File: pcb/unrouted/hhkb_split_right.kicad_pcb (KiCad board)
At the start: 2 copper layers, 173.7 x 97.4 mm, 83 parts, among them SW1 6, SW10 Y, SW11 U, SW12 I, SW13 O, SW14 P, SW15 [, SW16 ], SW17 Del, SW18 H, SW19 J, SW2 7, SW20 K, SW21 L, SW22 ;, SW23 ', SW24 Enter, SW25 N, SW26 M, SW27 ,, SW28 ., SW29 /, SW3 8, SW30 Shift, SW31 Fn, SW32 R-Space, SW33 Meta, SW34 Alt, SW4 9, SW5 0, SW6 -, SW7 =, SW8 \, SW9 `, U1 74LVC595, U2 74LVC595

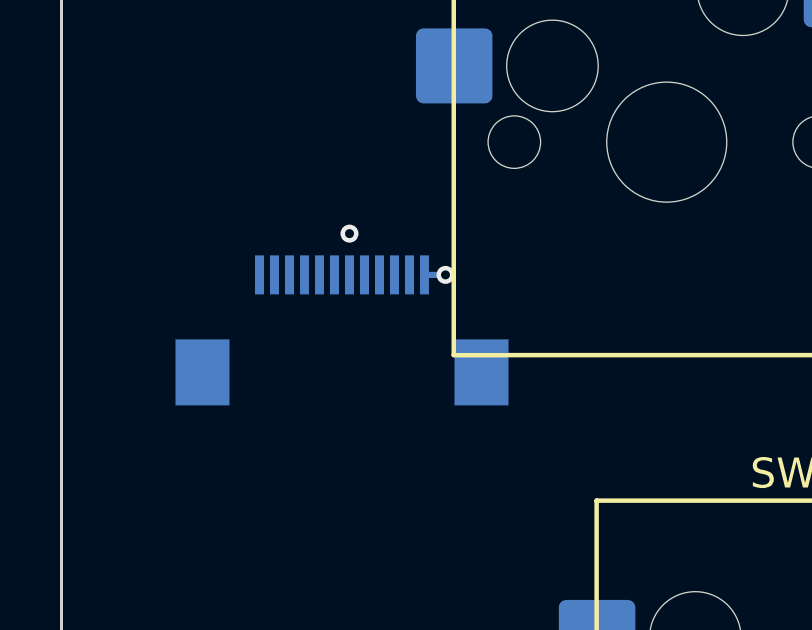
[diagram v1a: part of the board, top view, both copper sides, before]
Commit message: FFC コネクタの X を子基板と揃えた（左 3.52 → 0.40mm・右 1.35 → 0.00mm）
本体基板の J_DB と子基板の J_MAIN は**どちらも口が手前を向いている**のに
X がずれていて、ずれたぶん FFC が横へ折れていた（利用者の指摘）。

**座標を手で書かず、子基板の中心から取る。**直書きだとキー配列や
ケースの幅が動いた日に黙ってずれる。そのため
inner_sign / battery_x_center / daughterboard_x_center を gen_case.py
（build123d 依存で KiCad の Python から読めない）から interface.py へ移し、
gen_case は再輸出だけにした。二重に持っていた DB_W も出所を 1 つにし、
WALL / BATT_X は突き合わせの assert を置いた。

揃えた先に部品が居ることがあるので、_snap_clear_of_courtyards が
当たらない最寄りへ逃がし、ずれ量を印字する（左は D12 が 0.36mm 掛かるので
+0.40mm、右は 0.00mm で完全一致）。**スイッチは障害物に数えない**——
実装面が違う（スイッチは表・コネクタは裏の SMD）ので重なってよく、
数えると右が 3.95mm 逃げて揃える前より悪くなる。

## 一緒に見つかった別のバグ

GUIDE_VIAS の V3V3 中継ビアが (72.75, 84.0) と直書きされていた。
J_DB が動いた瞬間、**V3V3 のパッド(76.10)から外れて ROW_B のパッド(72.60)
の上に乗り**、ROW_B が未配線になる。パッドから座標を取るようにした。
これは移設前から潜在していたもので、実際にベースラインの右基板は
未配線 2 件（ROW_B と GND 離島）だった。

## 検証

- 再生成 → 自動配線 → DRC: 左 0/0・右 違反 0/未配線 1・子基板 0/0
  右の 1 件は U1 の GND 離島で、**ベースラインにもあった**（2 → 1 に減った）。
  コネクタ位置と無関係な既存の不具合なので範囲を広げず残す
- ずれ量は pcb_parts.json を取り直したうえで**実 STEP 形状から実測**
- gen_assembly の実形状の干渉 0 / refresh_view.sh で .blend も出し直し
- pytest tools: 437 passed / 3 failed。**3 件とも着手前から赤**
  （SPARE ネット 2 件は stash して確認済み、右の未配線 1 件は上記）

Co-Authored-By: Claude Opus 5 (1M context) <noreply@anthropic.com>
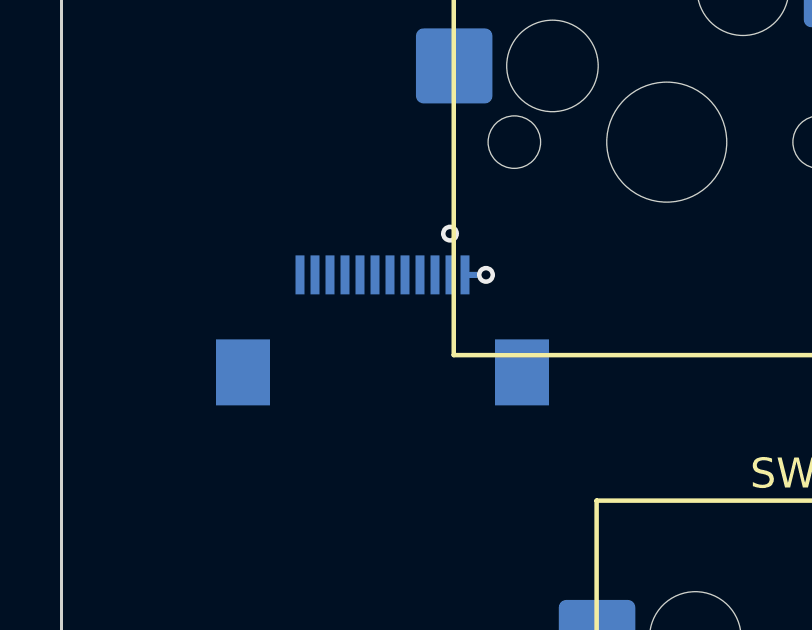
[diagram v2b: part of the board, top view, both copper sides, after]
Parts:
- moved J_DB 1.35 mm to (73.8, 87.2)

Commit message: 右の行とレーンの対応を左の鏡像に直した（ROW_A が最遠の行まで降りていた）
J_DB のパッド列は扇の根元で、外側(#12)を通る芯線が遠い行へ、内側(#8)が
近い行へ行くと交差しない。右はこの向きが左と同じままで、ROW_A(#8・最も
内側)が最遠の行(y=138.45)まで斜めに降り、ROW_E(#12)が束の真ん中に来て
いた。右の row-gpios を組み替えて、パッドの外側ほど遠い行になるようにした。

  #8 ROW_A → 行y 81.30 (コネクタから 4.08)
  #9 ROW_B → 100.35 (14.97)
  #10 ROW_C → 62.25 (23.12)
  #11 ROW_D → 119.40 (34.03)
  #12 ROW_E → 138.45 (53.07)

左は逆向きの単調で無変更。ネット名(#8=ROW_A…#12=ROW_E)は左右で同じで、
動かしたのは「どのレーンがどの行に載るか」だけ。circuit.py の J_DB は共通。

**未配線が 0 → 2 になったが、数字が悪いほうが正しい。**前の並びは未配線 0
だったが、扇が交差したまま通っていただけ。未配線 0 を根拠に戻さないこと。
残りは ROW_D(#11 → 行3) と GND(C_U2 のパッド 2 → ベタ・ROW とは別件)。

右の overlay には 2026-08-15 から「左とは意味が逆なので並びも逆になる」と
書いてあったが、実装が追随しておらず左と同一だった。文書だけが正しかった。

Co-Authored-By: Claude Opus 5 (1M context) <noreply@anthropic.com>
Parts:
- C_U1, C_U2: value cap_100n -> 100nF
- J_DB: value ffc_12p -> FH12-12S-0.5SH(55)
- SW1: value 6 -> CPG151101S11-2
- SW10: value Y -> CPG151101S11-2
- SW11: value U -> CPG151101S11-2
- SW12: value I -> CPG151101S11-2
- SW13: value O -> CPG151101S11-2
- SW14: value P -> CPG151101S11-2
- SW15: value [ -> CPG151101S11-2
- SW16: value ] -> CPG151101S11-2
- SW17: value Del -> CPG151101S11-2
- SW18: value H -> CPG151101S11-2
- SW19: value J -> CPG151101S11-2
- SW2: value 7 -> CPG151101S11-2
- SW20: value K -> CPG151101S11-2
- SW21: value L -> CPG151101S11-2
- SW22: value ; -> CPG151101S11-2
- SW23: value ' -> CPG151101S11-2
- SW24: value Enter -> CPG151101S11-2
- SW25: value N -> CPG151101S11-2
- SW26: value M -> CPG151101S11-2
- SW27: value , -> CPG151101S11-2
- SW28: value . -> CPG151101S11-2
- SW29: value / -> CPG151101S11-2
- SW3: value 8 -> CPG151101S11-2
- SW30: value Shift -> CPG151101S11-2
- SW31: value Fn -> CPG151101S11-2
- SW32: value R-Space -> CPG151101S11-2
- SW33: value Meta -> CPG151101S11-2
- SW34: value Alt -> CPG151101S11-2
- SW4: value 9 -> CPG151101S11-2
- SW5: value 0 -> CPG151101S11-2
- SW6: value - -> CPG151101S11-2
- SW7: value = -> CPG151101S11-2
- SW8: value \ -> CPG151101S11-2
- SW9: value ` -> CPG151101S11-2
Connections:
- D10 pad 1: ROW_E -> ROW_A
- D11 pad 1: ROW_E -> ROW_A
- D12 pad 1: ROW_E -> ROW_A
- D13 pad 1: ROW_E -> ROW_A
- D14 pad 1: ROW_E -> ROW_A
- D15 pad 1: ROW_E -> ROW_A
- D16 pad 1: ROW_E -> ROW_A
- D17 pad 1: ROW_E -> ROW_A
- D18 pad 1: ROW_D -> ROW_B
- D19 pad 1: ROW_D -> ROW_B
- D20 pad 1: ROW_D -> ROW_B
- D21 pad 1: ROW_D -> ROW_B
- D22 pad 1: ROW_D -> ROW_B
- D23 pad 1: ROW_D -> ROW_B
- D24 pad 1: ROW_D -> ROW_B
- D25 pad 1: ROW_B -> ROW_D
- D26 pad 1: ROW_B -> ROW_D
- D27 pad 1: ROW_B -> ROW_D
- D28 pad 1: ROW_B -> ROW_D
- D29 pad 1: ROW_B -> ROW_D
- D30 pad 1: ROW_B -> ROW_D
- D31 pad 1: ROW_B -> ROW_D
- D32 pad 1: ROW_A -> ROW_E
- D33 pad 1: ROW_A -> ROW_E
- D34 pad 1: ROW_A -> ROW_E
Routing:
- net ROW_E: track 138.1 -> 66.7 mm
- net ROW_A: track 66.7 -> 138.1 mm
- net ROW_D: track 126.2 -> 128.6 mm
- net ROW_B: track 128.6 -> 126.2 mm

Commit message: 右の段 1 の列割り当てを規則的に直した（配線ルールは触らない）
利用者「右は、まず配線ルールは基本いじらずに、まずは列割り当てを
直しましょう。明らかに規則的じゃない」。

**測ったら、4 段のうち段 1 だけが不規則だった。**

段 1（Y U I O P [ ] Del）は列 8 を飛ばして 6,7,9,10,11,12,13,14 に
していた。**8 キーとも 1u で等間隔なのに途中で 1 つ飛ばすと、I 以降が
全部 1 列ぶん右にずれる**。実測で 2 キーが「キーの真上を通らない列」に
繋がっていた:

    P  範囲 257.2〜276.2  真上は COL10 だけ  なのに COL11(276.2)
    [  範囲 276.2〜295.3  真上は COL11 だけ  なのに COL12(295.3)

**6〜12 を連続で使い、空けるのは 13** に変更。これで 8 キーとも真上の
列に乗る（6/8 → 8/8）。Del だけ 1.5u で右端に寄るので COL14。

**他の段（2/3/4）は総当りで測った結果すでに最良**で、飛ばしている列は
幅広キー（Enter 2.25u / Shift 1.75u / R-Space 3u）による本物の欠番
だった。**触らない。**

配線ルールは 1 文字も変えていない。それでも割り当てを直しただけで
**引けなかったホップが 4 → 3 に減った**（右: 列 83 → 92 区間）。
配線由来の DRC 違反 0。残る未接続はマトリクス内 2 件（COL7/COL8）と
GND の島 1 件。

左は変化なし（段 1 は右だけの行。指紋で確認して戻した）。

Co-Authored-By: Claude Opus 5 (1M context) <noreply@anthropic.com>
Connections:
- SW12 pad 1: COL3 -> COL2
- SW13 pad 1: COL4 -> COL3
- SW14 pad 1: COL5 -> COL4
- SW15 pad 1: COL6 -> COL5
- SW16 pad 1: COL7 -> COL6

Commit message: 右の列を「行内の順番＝列番号」にした（利用者の指定）
利用者「SW1, 10, 18, 25, 32 を Col 0 として。以降、その行を一つ右に
いくごとに列を増やして」「ただし SW33, 34 は例外」。

各行の左端が COL0、以降 +1。**飛ばさない。**以前は段ごとに開始列も
欠番もばらばらで（段2 は列 7 から、段4 は列 8 から、SW17 が COL8、
SW30 が COL7）、「行内の位置」と「列番号」が対応していなかった。

例外の SW33/SW34 は、実測でキーの真上を通る列に合わせた（確認済み）:
    SW33 Meta  範囲 247.65〜276.23 → COL3（x=261.94 と完全一致）
    SW34 Alt   範囲 276.23〜295.27 → COL4（ずれ 4.76mm）

**配線ルールは 1 文字も変えていない。**割り当てだけで、引けなかった
ホップが **4 → 2**、マトリクス内の未接続が **3 → 1** に減った
（右: 列 88 区間・橋のビア 38 個・配線由来の DRC 違反 0）。

## 検査を 1 つ作り直した

`test_matrix_columns_follow_physical_position`（同じ列のキーが x 方向に
1.5 キー幅以内）は、**この方針では必ず落ちる**——各行の左端が COL0 に
なるので同じ列が 38mm 散らばる。

**落ちるから外す、はしない。**守りたかったのは x の散らばりではなく
「長い横断が生まれないこと」（38mm の横断で DRC が交差を出した事故から
書かれた検査）なので、**そちらを直接測る**ように書き換えた
（`test_matrix_columns_do_not_need_long_crossings`）。実測の最長は
左 16.7mm / 右 20.2mm で、1 段ぶんの斜め（26.9mm）以内。

⚠️ **途中、正規表現が `(net <番号>)` を探していて 1 本も拾えず、
閾値を 15mm に下げても通っていた。**`(segment ...)` はネットを名前で
持つ。書式を実物で確かめて直し、**閾値を下げると落ちること**を
確認した（16.7 / 20.2mm が正しく出る）。読めなかったら落ちる
assert も足した。

本番の `pcb/` は古い割り当てのままなので
`test_matrix_wiring_matches_the_firmware` が赤。**意図した状態**として
open-gaps #47 に記録した（残り 6 件の赤は私の変更前から）。

Co-Authored-By: Claude Opus 5 (1M context) <noreply@anthropic.com>
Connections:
- SW17 pad 1: COL8 -> COL7
- SW18 pad 1: COL1 -> COL0
- SW19 pad 1: COL2 -> COL1
- SW20 pad 1: COL3 -> COL2
- SW21 pad 1: COL4 -> COL3
- SW22 pad 1: COL5 -> COL4
- SW23 pad 1: COL6 -> COL5
- SW24 pad 1: COL7 -> COL6
- SW25 pad 1: COL1 -> COL0
- SW26 pad 1: COL2 -> COL1
- SW27 pad 1: COL3 -> COL2
- SW28 pad 1: COL4 -> COL3
- SW29 pad 1: COL5 -> COL4
- SW30 pad 1: COL7 -> COL5
- SW31 pad 1: COL8 -> COL6
- SW32 pad 1: COL2 -> COL0
- SW33 pad 1: COL4 -> COL3
- SW34 pad 1: COL5 -> COL4

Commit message: 右のマトリクスを完成させた（U1/U2 の移動を取り込み・引き残し 0）
利用者が基板上で U2 と U1 を動かした:
  「SW6 から SW15 は U2 をずらしたので、それで試してください」
  「SW16-24 は工夫して」
  「SW5, 6 だけど、他の同じ行の配線パターンを踏襲して」
  「コンデンサとか避けておいたので」

**U1/U2 の移動を生成器へ取り込んだ**（座標が完全一致することを確認）:
  U2  帯0 x=+15.0    → 帯1 x=-40.662 dy=+0.725  (109.338, 88.900)
  U1  帯0 x=+2.0     → 帯3 x=-75.938 dy=-0.025  ( 74.062,126.250)

どちらも**列の通り道を塞いでいた**。U2 は COL5（SW6→SW15）を、
U1 と C_U1 は COL4（x≈146〜152）を。移動で両方とも素直に降りられる。

**SW5 が同じ段の他と揃った**（利用者の指摘）。SW4/SW5/SW6 が
「0.200mm 降りて曲がり、75.650 で 45° を終える」と完全に同じ形。
前は SW5 だけ 3.700mm 降りていた（U1/C_U1 を避けるため）。

**SW16→SW24（ST24 のスタビ穴）は形 F で解いた。**C も D も曲がる y が
1 点に決まっており、そこが穴の真横だと 0.289mm しか空かない。
**曲がる高さを振れる形**を足すと、45° を保ったまま穴の左を抜けて
1.030mm 取れる（他の列と同じ値）。

2 つ直した:
  - 橋を架ける枝でも**余裕が最大の候補を採る**（他の枝は済んでいた）
  - `gen_matrix` が **GND の離島を繋いでいなかった**。配線が密になって
    ベタが割れ、DRC が「ゾーンが繋がっていない」を 2 件出した。
    本番と同じ `gnd_fanout.stitch_islands` を呼ぶ（左 10 個・右 12 個）。
    浮いた銅は 2.4GHz でアンテナになる

左右とも: **引かなかったホップ 0 / 配線由来の DRC 違反 0 /
マトリクス内の未接続 0 / 最小の隙間 1.030mm**。

⚠️ **C_U1 は取り込んでいない。**利用者の板では U1 から 136mm 離れており、
パスコンとして効かない位置（効くのは往復ループのインダクタンス）。
`DECOUPLE_BESIDE` が U1 から算出する仕組みのまま残した。

pytest の赤 8 件は**私の変更の前後で同じ**（本番 pcb/ が未再生成＝
open-gaps #47、SPARE 系は以前から）。

Co-Authored-By: Claude Opus 5 (1M context) <noreply@anthropic.com>
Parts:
- moved C_U1 96.6 mm to (68.2, 126.2)
- moved U1 96.6 mm to (74.1, 126.2)
- moved C_U2 59.1 mm to (103.4, 88.9)
- moved U2 59.1 mm to (109.3, 88.9)

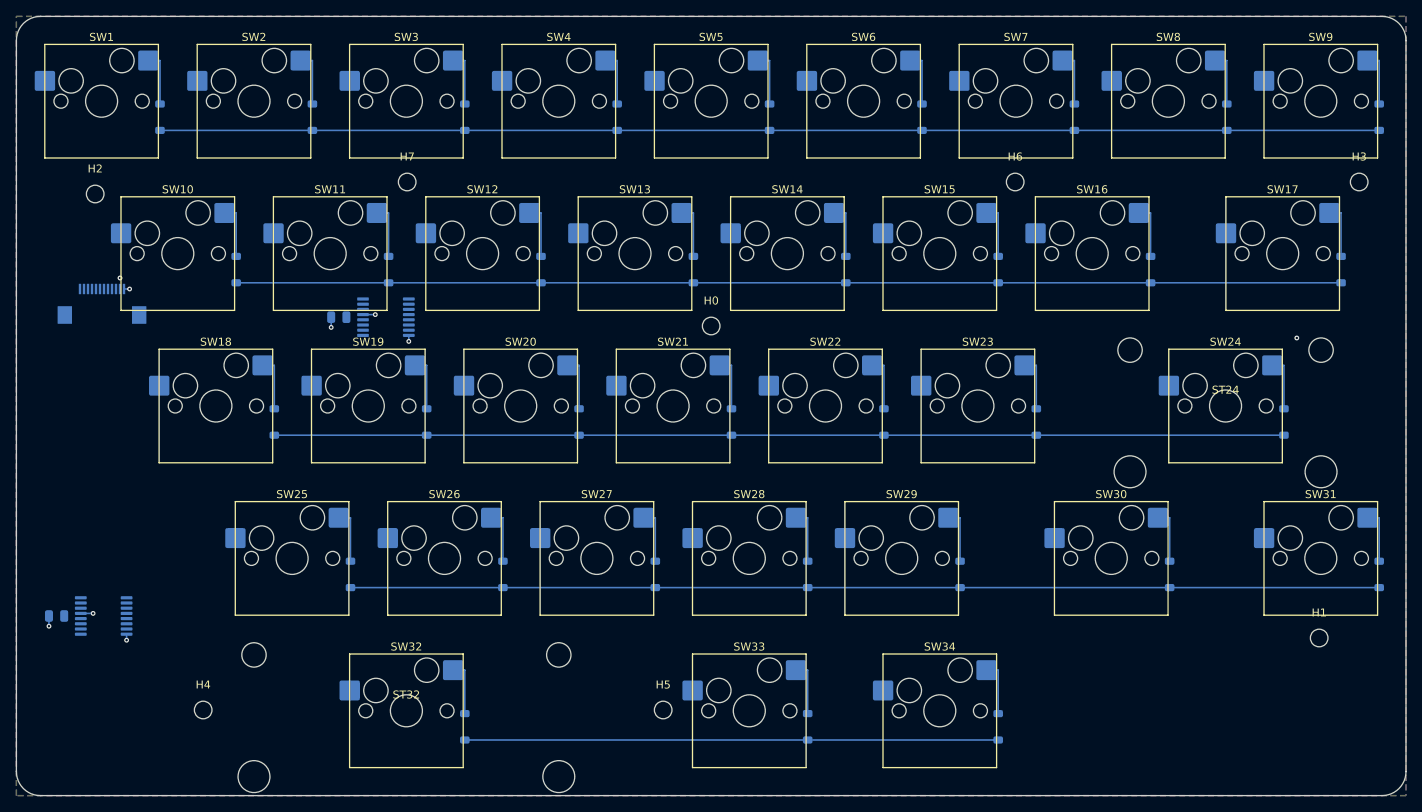
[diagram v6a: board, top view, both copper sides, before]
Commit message: キーマトリクスの配線を凍結した（自動配線の前に機械で引く）
利用者「このキーマトリクスの配線を凍結させてください。基本的にはこの
配線は変更せず、自動配線の前に機械的に配線しておく形にしておいて」。

  gen_pcb   … 列のバスも引く（行・SW→D に続いて 3 つ目）。
              左 99 区間 / 右 119 区間・**全ホップ**
  autoroute … SES 取り込みのあと `replay_matrix` で
              **未配線の板からそのまま写す**

## 「引き直す」ではなく「写す」にした理由

最初は取り込み後に `prewire_col_bus` を呼び直す形にした。**13 ホップが
「障害物」で落ちた。**経路は板の上にある物から決まるが、取り込み後は
ビアが 38 → 1217 個に増えている（gnd_fanout）。**同じ手順を回しても
同じ答えにならない。**

**凍結とは同じ手順を回すことではなく、同じ結果を置き直すこと。**
未配線の板が唯一の出どころで、そこに gen_pcb が引いた線が残っている。
実測で **209 個中 209 個が完全一致**（差分は両方向ともゼロ）。

## 注記と実物が食い違っていたのを直した

`_strip_prewired` の説明は「ROW は `(type protect)` で渡してある」と
書いていたが、**実際は `type route` のままだった**（COL も同じ）。
上の置換は「消したネット」にしか掛からず、消さない ROW/COL には
効いていなかった。`FROZEN` を足して明示的に protect にする。
ROW/COL をネットごと消せないのは、最後の 1 本（ROW は J_DB、
COL は U1）だけは Freerouting に引かせるため。

## 置き換えたものを消した

`tools/gen_matrix.py` と `pcb/matrix/` を削除（役目を gen_pcb が継いだ）。
長い横断の検査は `pcb/unrouted/` を見るように変更——**形が決まるのは
そこ**で、本番はその写し。消した名前で grep して残骸 0 を確認。
故意に閾値を下げて、検査が効いていることも確認（16.7 / 20.2mm）。

⚠️ **本番の pcb/ はまだ作り直していない**（利用者「本番配線はまだ。
U1, U2 の場所や配線が決まってから」）。open-gaps #47 を現状に合わせて
書き直した。pytest の赤 8 件は私の変更前と同じ顔ぶれ。

Co-Authored-By: Claude Opus 5 (1M context) <noreply@anthropic.com>
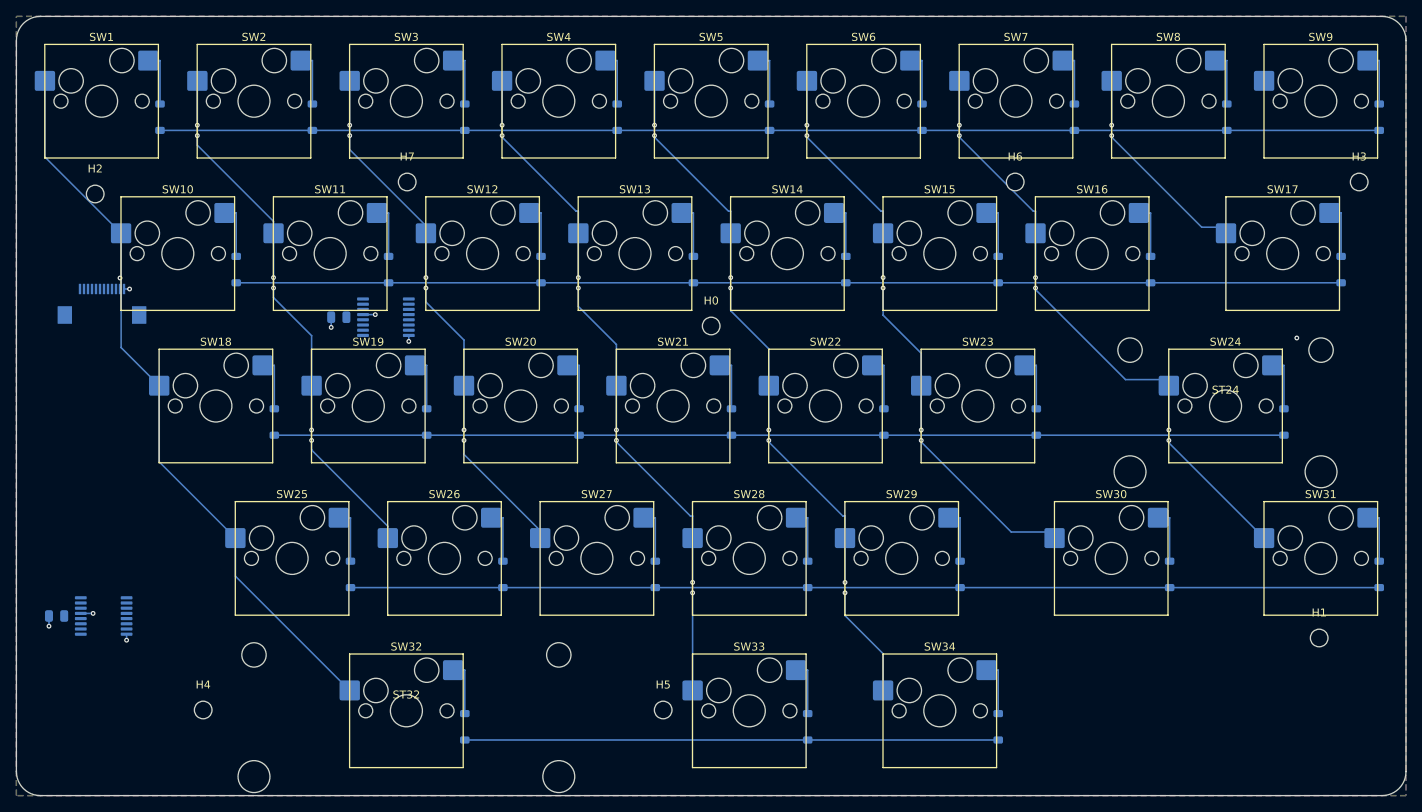
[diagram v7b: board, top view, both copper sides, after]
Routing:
- net COL0: track 0.00 -> 92.0 mm
- net COL4: track 0.00 -> 88.4 mm, vias 0 -> 8
- net COL3: track 0.00 -> 86.4 mm, vias 0 -> 8
- net COL6: track 0.00 -> 76.3 mm, vias 0 -> 6
- net COL5: track 0.00 -> 73.3 mm, vias 0 -> 6
- net COL2: track 0.00 -> 67.0 mm, vias 0 -> 6
- net COL1: track 0.00 -> 67.0 mm, vias 0 -> 6
- net COL7: track 0.00 -> 26.7 mm, vias 0 -> 2

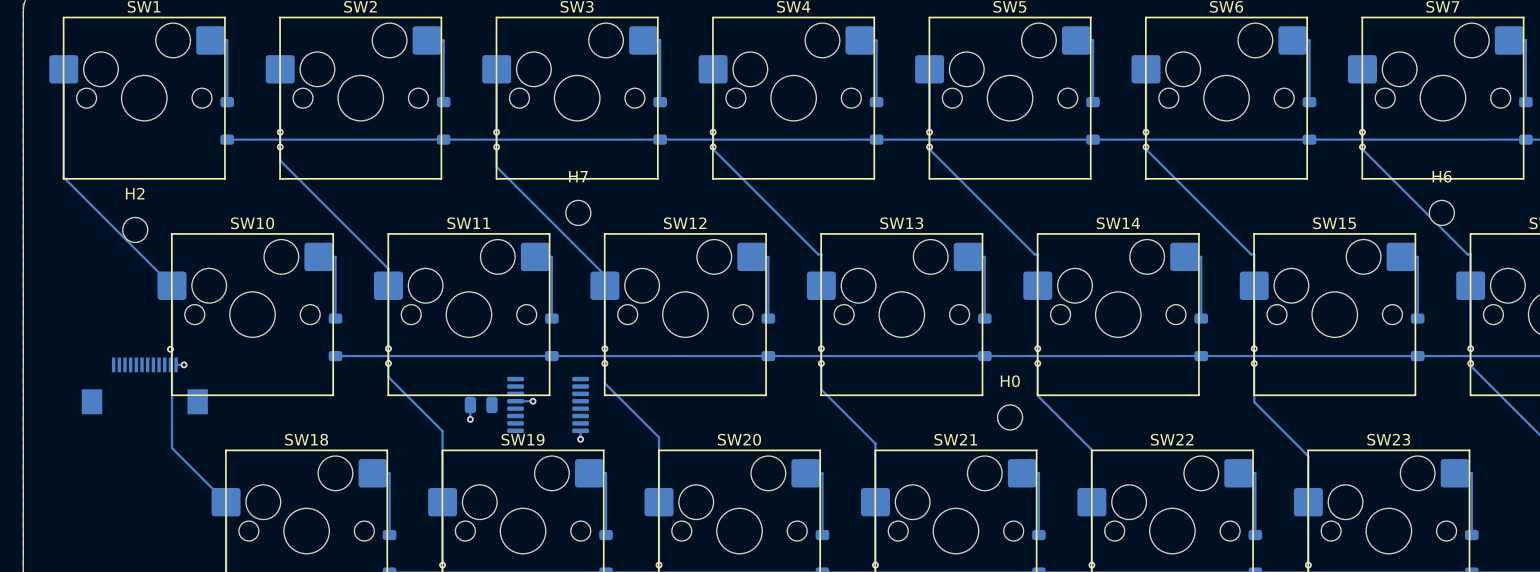
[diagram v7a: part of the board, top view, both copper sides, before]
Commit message: 列のバスを部品より後に引く（凍結の欠陥を直した）
利用者「COL0 の配線が変わっている。凍結したはずなのに、J_DB と U1 と
干渉するように変わっている」。

**COL0 の座標は 1 つも変わっていなかった**（8 本とも一致。凍結は
効いている）。しかし**凍結した配線が J_DB に食い込んでいた**ので、
「干渉するように変わっている」という見立ては正しかった。

## 原因は生成の順番

    （前） 列のバスを引く → J_DB/U1/U2 を置く → 取付穴を置く
    （後） J_DB/U1/U2 を置く → 取付穴を置く → 列のバスを引く

`prewire_col_bus` は板の上にある物を見て経路を決めるのに、
**呼ばれた時点で J_DB も U1 も取付穴もまだ板に無かった。**
衝突検査は正しく書けていたが、**見るべき相手が存在していなかった。**

実測（直す前）:
    右 COL0 ↔ J_DB の V3V3 パッド   0.140mm（要 1.017mm）… 短絡
    左 COL3 ↔ H0 の取付穴          -0.487mm
    右 COL6 ↔ H6 の取付穴          -0.221mm

⚠️ **凍結をコミットしたとき「全ホップ・最小の隙間 1.030mm」と報告したが
誤りだった。**その数字は穴とスイッチのパッドしか含んでおらず、J_DB は
最初から食い込んでいた。**検査対象に入っていない部品は、検査していない
のと同じ。**

## 直したあと

    COL と全パッドの最小の余裕: 左 +1.030mm / 右 +0.981mm
    引かなかったホップ 0（左 103 / 右 122 区間）
    未配線の板の DRC: 左 0 件 / 右 2 件（guide_vias の中継ビアが
    片側だけ繋がっている状態。本番配線で繋がる）

U1/U2 の位置は**この commit に含めない**（利用者が検討中）。順番を
直しただけで、U1/U2 が元の位置のままでも干渉は解けた。

pytest の赤 6 件は私の変更前と同じ（本番 pcb/ が未再生成＝#47）。

Co-Authored-By: Claude Opus 5 (1M context) <noreply@anthropic.com>
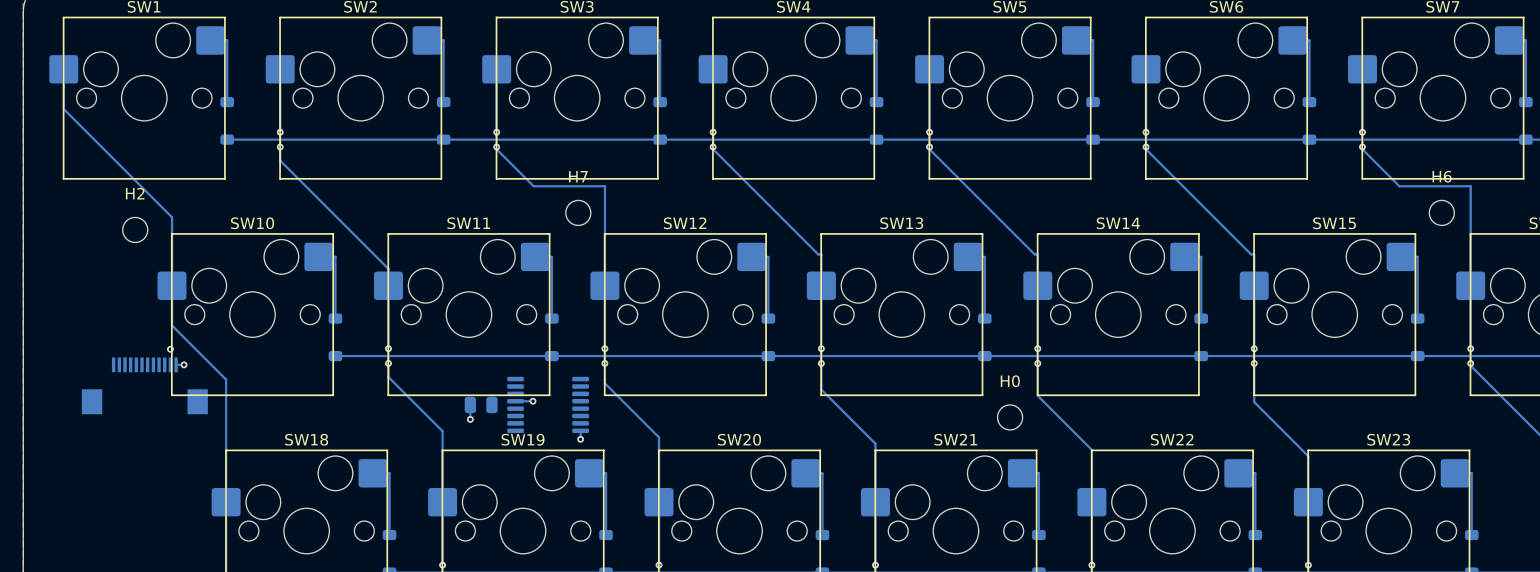
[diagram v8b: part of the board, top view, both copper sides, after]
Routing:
- net COL2: track 67.0 -> 70.7 mm
- net COL6: track 76.3 -> 79.8 mm
